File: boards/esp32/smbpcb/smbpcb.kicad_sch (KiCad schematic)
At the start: 61 parts, among them IC1 MiCS-6814, J1 USB_B_Micro, J2 PMS7003, Q1 SUD08P06-155L, SW1 RESET, SW2 RESET, U1 MCP73831-2-OT, U2 SGM6603-5.0YN6G_TR, U3 ESP32-WROOM-32, U4 SSD1306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

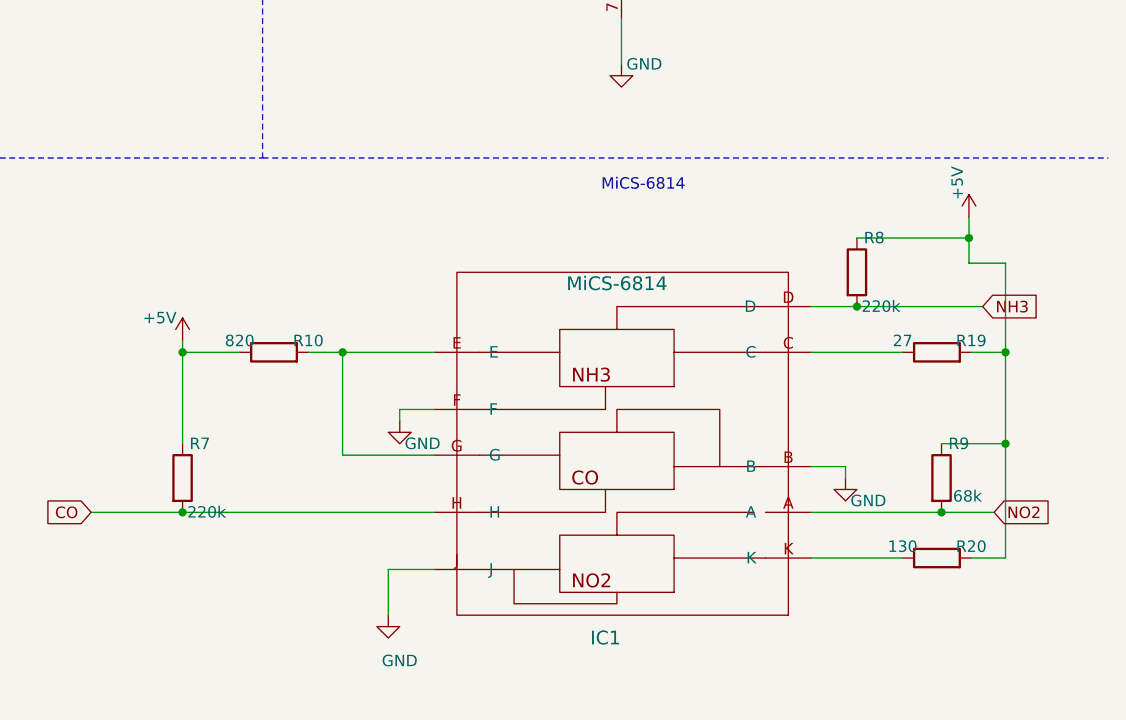
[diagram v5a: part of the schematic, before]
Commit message: fixed mics pullups
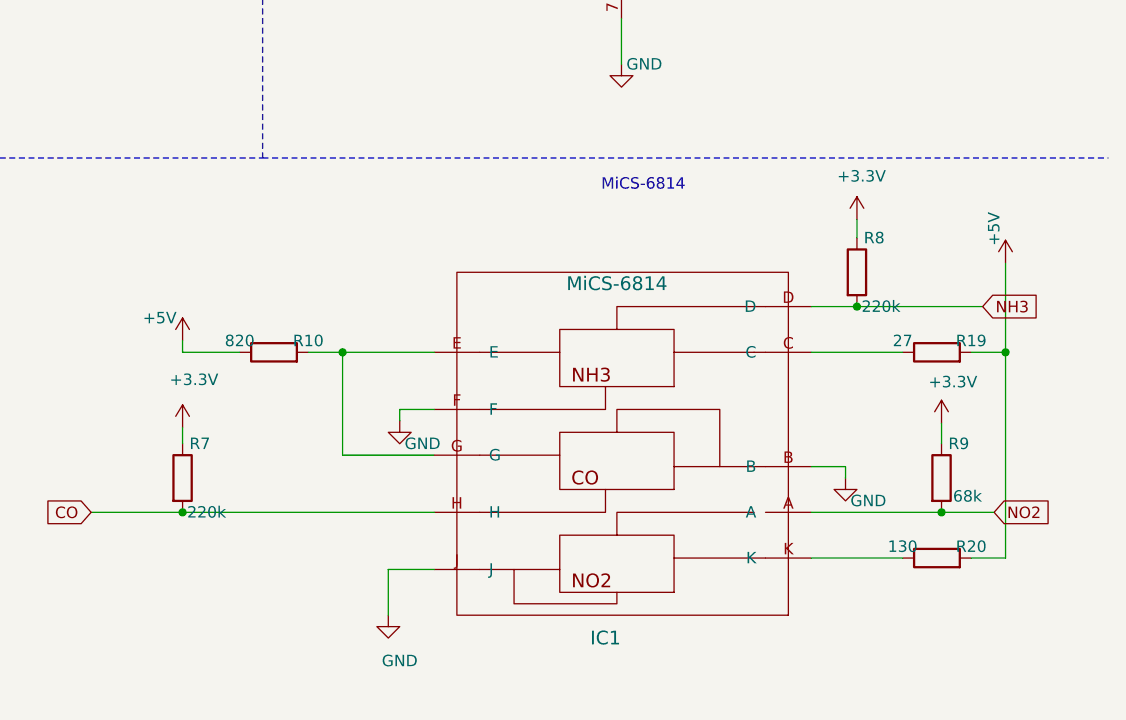
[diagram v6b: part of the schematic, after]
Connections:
- net +3V3: now also R7.1, R8.1, R9.1
- net +5V: no longer R7.1, R8.1, R9.1
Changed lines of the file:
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@@
   (junction (at 298.196 83.82) (diameter 0.9144) (color 0 0 0 0))
   (junction (at 303.276 83.82) (diameter 0.9144) (color 0 0 0 0))
-  (junction (at 307.34 173.99) (diameter 0.9144) (color 0 0 0 0))
   (junction (at 307.34 191.77) (diameter 0.9144) (color 0 0 0 0))
   (junction (at 325.12 173.99) (diameter 0.9144) (color 0 0 0 0))
@@
   (junction (at 390.906 53.34) (diameter 0.9144) (color 0 0 0 0))
   (junction (at 391.668 191.77) (diameter 0.9144) (color 0 0 0 0))
-  (junction (at 394.716 161.29) (diameter 0.9144) (color 0 0 0 0))
   (junction (at 398.78 173.99) (diameter 0.9144) (color 0 0 0 0))
-  (junction (at 398.78 184.15) (diameter 0.9144) (color 0 0 0 0))
   (no_connect (at 143.51 135.89))
   (no_connect (at 153.67 135.89))
@@
     (stroke (width 0) (type solid) (color 0 0 0 0))
   )
-  (wire (pts (xy 307.34 173.99) (xy 307.34 184.15))
+  (wire (pts (xy 307.34 182.372) (xy 307.34 184.15))
     (stroke (width 0) (type solid) (color 0 0 0 0))
   )
@@
     (stroke (width 0) (type solid) (color 0 0 0 0))
   )
-  (wire (pts (xy 382.27 161.29) (xy 394.716 161.29))
+  (wire (pts (xy 382.27 159.258) (xy 382.27 161.29))
     (stroke (width 0) (type solid) (color 0 0 0 0))
   )
@@
     (stroke (width 0) (type solid) (color 0 0 0 0))
   )
-  (wire (pts (xy 391.668 184.15) (xy 398.78 184.15))
+  (wire (pts (xy 391.668 181.864) (xy 391.668 184.15))
     (stroke (width 0) (type solid) (color 0 0 0 0))
   )
@@
     (stroke (width 0) (type solid) (color 0 0 0 0))
   )
-  (wire (pts (xy 394.716 159.004) (xy 394.716 161.29))
-    (stroke (width 0) (type solid) (color 0 0 0 0))
-  )
-  (wire (pts (xy 394.716 161.29) (xy 394.716 164.084))
-    (stroke (width 0) (type solid) (color 0 0 0 0))
-  )
   (wire (pts (xy 394.97 173.99) (xy 398.78 173.99))
     (stroke (width 0) (type solid) (color 0 0 0 0))
@@
     (stroke (width 0) (type solid) (color 0 0 0 0))
   )
-  (wire (pts (xy 398.78 164.084) (xy 394.716 164.084))
-    (stroke (width 0) (type solid) (color 0 0 0 0))
-  )
   (wire (pts (xy 398.78 173.99) (xy 398.78 164.084))
     (stroke (width 0) (type solid) (color 0 0 0 0))
   )
-  (wire (pts (xy 398.78 173.99) (xy 398.78 184.15))
-    (stroke (width 0) (type solid) (color 0 0 0 0))
-  )
-  (wire (pts (xy 398.78 184.15) (xy 398.78 196.85))
+  (wire (pts (xy 398.78 173.99) (xy 398.78 196.85))
     (stroke (width 0) (type solid) (color 0 0 0 0))
   )
@@
     (pin "1")
   )
+  (symbol (lib_id "power:+3.3V") (at 307.34 182.372 0) (unit 1)
+    (in_bom yes) (on_board yes)
+    (property "Reference" "#PWR?" (id 0) (at 307.34 186.182 0)
+      (effects (font (size 1.27 1.27)) hide)
+    )
+    (property "Value" "+3.3V" (id 1) (at 308.61 177.038 0))
+    (property "Footprint" "" (id 2) (at 307.34 182.372 0)
+      (effects (font (size 1.27 1.27)) hide)
+    )
+    (property "Datasheet" "" (id 3) (at 307.34 182.372 0)
+      (effects (font (size 1.27 1.27)) hide)
+    )
+    (pin "1")
+  )
   (symbol (lib_id "power:+3V3") (at 354.33 21.59 0) (unit 1)
     (in_bom yes) (on_board yes)
@@
     (pin "1")
   )
-  (symbol (lib_id "power:+5V") (at 394.716 159.004 0) (unit 1)
+  (symbol (lib_id "power:+3.3V") (at 382.27 159.258 0) (unit 1)
+    (in_bom yes) (on_board yes)
+    (property "Reference" "#PWR?" (id 0) (at 382.27 163.068 0)
+      (effects (font (size 1.27 1.27)) hide)
+    )
+    (property "Value" "+3.3V" (id 1) (at 382.778 154.432 0))
+    (property "Footprint" "" (id 2) (at 382.27 159.258 0)
+      (effects (font (size 1.27 1.27)) hide)
+    )
+    (property "Datasheet" "" (id 3) (at 382.27 159.258 0)
+      (effects (font (size 1.27 1.27)) hide)
+    )
+    (pin "1")
+  )
+  (symbol (lib_id "power:+3.3V") (at 391.668 181.864 0) (unit 1)
     (in_bom yes) (on_board yes)
-    (property "Reference" "#PWR0117" (id 0) (at 394.716 162.814 0)
+    (property "Reference" "#PWR?" (id 0) (at 391.668 185.674 0)
       (effects (font (size 1.27 1.27)) hide)
     )
-    (property "Value" "+5V" (id 1) (at 393.446 155.194 90))
-    (property "Footprint" "" (id 2) (at 394.716 159.004 0)
+    (property "Value" "+3.3V" (id 1) (at 392.938 177.292 0))
+    (property "Footprint" "" (id 2) (at 391.668 181.864 0)
       (effects (font (size 1.27 1.27)) hide)
     )
-    (property "Datasheet" "" (id 3) (at 394.716 159.004 0)
+    (property "Datasheet" "" (id 3) (at 391.668 181.864 0)
+      (effects (font (size 1.27 1.27)) hide)
+    )
+    (pin "1")
+  )
+  (symbol (lib_id "power:+5V") (at 398.78 164.084 0) (unit 1)
+    (in_bom yes) (on_board yes)
+    (property "Reference" "#PWR0117" (id 0) (at 398.78 167.894 0)
+      (effects (font (size 1.27 1.27)) hide)
+    )
+    (property "Value" "+5V" (id 1) (at 397.51 160.274 90))
+    (property "Footprint" "" (id 2) (at 398.78 164.084 0)
+      (effects (font (size 1.27 1.27)) hide)
+    )
+    (property "Datasheet" "" (id 3) (at 398.78 164.084 0)
       (effects (font (size 1.27 1.27)) hide)
     )
@@
       (effects (font (size 1.27 1.27)) hide)
     )
-    (property "Mouser" "ST-1102W-4.3" (id 4) (at 146.05 167.005 0)
+    (property "Mouser" "ST-1102W-4.3" (id 5) (at 146.05 167.005 0)
       (effects (font (size 1.27 1.27)) hide)
     )
@@
       (effects (font (size 1.27 1.27)) hide)
     )
-    (property "Mouser" "ST-1102W-4.3" (id 4) (at 186.055 168.91 0)
+    (property "Mouser" "ST-1102W-4.3" (id 5) (at 186.055 168.91 0)
       (effects (font (size 1.27 1.27)) hide)
     )
@@
       (reference "#PWR0134") (unit 1) (value "GND") (footprint "")
     )
+    (path "/2582b681-97c1-4fd5-b2de-561f4f59d48d"
+      (reference "#PWR?") (unit 1) (value "+3.3V") (footprint "")
+    )
+    (path "/87f29081-f5c6-4e96-b2bd-d8dcab406213"
+      (reference "#PWR?") (unit 1) (value "+3.3V") (footprint "")
+    )
+    (path "/9b025ca2-fd0f-474f-9b18-35df1cec7e3a"
+      (reference "#PWR?") (unit 1) (value "+3.3V") (footprint "")
+    )
     (path "/cbb17be5-135d-4808-9aa3-a561edb7c072"
